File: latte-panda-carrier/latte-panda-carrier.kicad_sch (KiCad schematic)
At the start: 6 parts

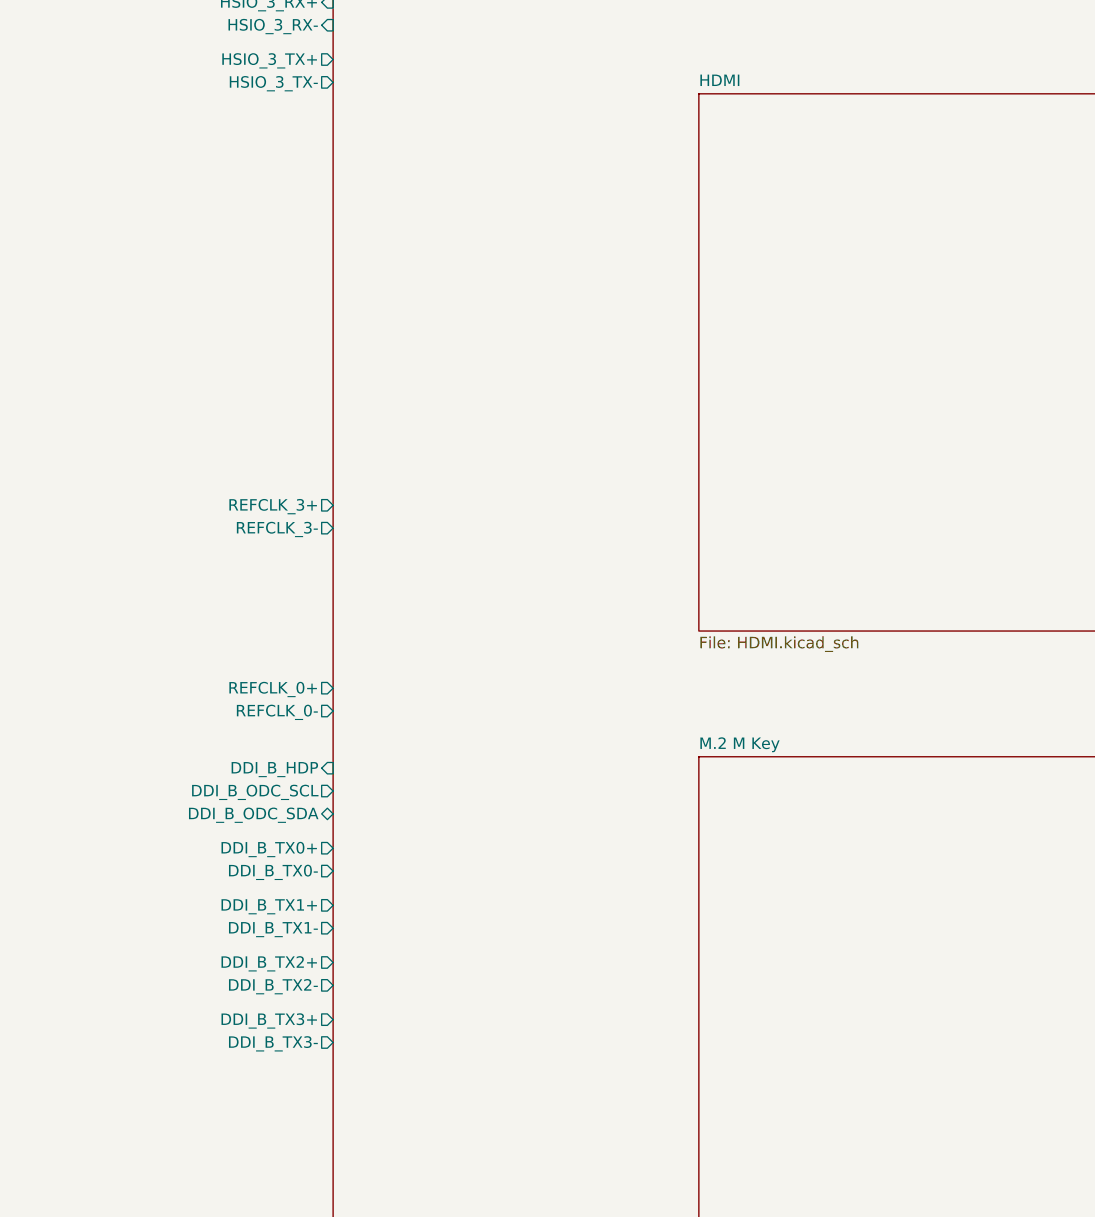
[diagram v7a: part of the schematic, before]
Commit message: 170.2
Add HDMI.
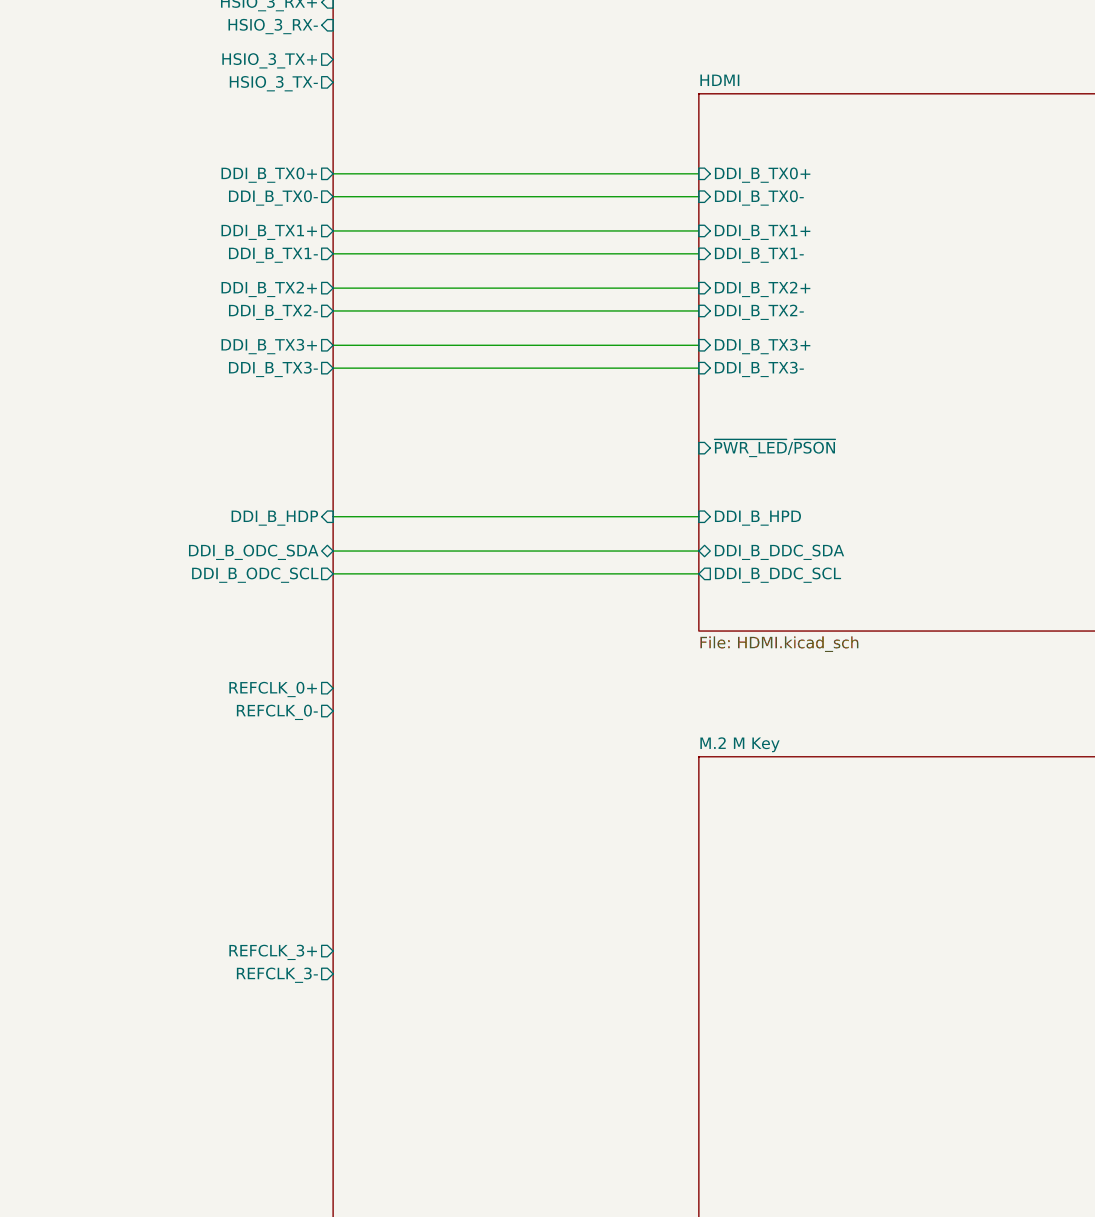
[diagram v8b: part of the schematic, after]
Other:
- sheet HDMI ports: added DDI_B_DDC_SCL, DDI_B_DDC_SDA, DDI_B_HPD, DDI_B_TX0+, DDI_B_TX0-, DDI_B_TX1+, DDI_B_TX1-, DDI_B_TX2+, DDI_B_TX2-, DDI_B_TX3+, DDI_B_TX3-, ~{PWR_LED}/~{PSON}; removed none
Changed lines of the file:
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@@
+	(wire
+		(pts
+			(xy 340.36 283.21) (xy 381 283.21)
+		)
+		(stroke
+			(width 0)
+			(type default)
+		)
+	)
 	(wire
 		(pts
@@
 	(wire
 		(pts
+			(xy 340.36 247.65) (xy 381 247.65)
+		)
+		(stroke
+			(width 0)
+			(type default)
+		)
+	)
+	(wire
+		(pts
 			(xy 340.36 154.94) (xy 381 154.94)
 		)
@@
 	(wire
 		(pts
+			(xy 340.36 243.84) (xy 381 243.84)
+		)
+		(stroke
+			(width 0)
+			(type default)
+		)
+	)
+	(wire
+		(pts
+			(xy 340.36 256.54) (xy 381 256.54)
+		)
+		(stroke
+			(width 0)
+			(type default)
+		)
+	)
+	(wire
+		(pts
 			(xy 184.15 156.21) (xy 217.17 156.21)
 		)
@@
 	(wire
 		(pts
+			(xy 340.36 250.19) (xy 381 250.19)
+		)
+		(stroke
+			(width 0)
+			(type default)
+		)
+	)
+	(wire
+		(pts
 			(xy 184.15 295.91) (xy 217.17 295.91)
 		)
@@
 	(wire
 		(pts
+			(xy 340.36 241.3) (xy 381 241.3)
+		)
+		(stroke
+			(width 0)
+			(type default)
+		)
+	)
+	(wire
+		(pts
 			(xy 184.15 207.01) (xy 217.17 207.01)
 		)
@@
 	(wire
 		(pts
+			(xy 340.36 279.4) (xy 381 279.4)
+		)
+		(stroke
+			(width 0)
+			(type default)
+		)
+	)
+	(wire
+		(pts
 			(xy 340.36 138.43) (xy 381 138.43)
 		)
@@
 	(wire
 		(pts
+			(xy 340.36 260.35) (xy 381 260.35)
+		)
+		(stroke
+			(width 0)
+			(type default)
+		)
+	)
+	(wire
+		(pts
 			(xy 340.36 158.75) (xy 381 158.75)
 		)
@@
 	(wire
 		(pts
+			(xy 340.36 262.89) (xy 381 262.89)
+		)
+		(stroke
+			(width 0)
+			(type default)
+		)
+	)
+	(wire
+		(pts
 			(xy 340.36 91.44) (xy 381 91.44)
 		)
@@
 	(wire
 		(pts
+			(xy 340.36 285.75) (xy 381 285.75)
+		)
+		(stroke
+			(width 0)
+			(type default)
+		)
+	)
+	(wire
+		(pts
 			(xy 184.15 163.83) (xy 217.17 163.83)
+		)
+		(stroke
+			(width 0)
+			(type default)
+		)
+	)
+	(wire
+		(pts
+			(xy 340.36 254) (xy 381 254)
 		)
 		(stroke
@@
 			)
 		)
+		(pin "DDI_B_DDC_SCL" output
+			(at 381 285.75 180)
+			(effects
+				(font
+					(size 1.27 1.27)
+				)
+				(justify left)
+			)
+		)
+		(pin "DDI_B_DDC_SDA" bidirectional
+			(at 381 283.21 180)
+			(effects
+				(font
+					(size 1.27 1.27)
+				)
+				(justify left)
+			)
+		)
+		(pin "DDI_B_HPD" input
+			(at 381 279.4 180)
+			(effects
+				(font
+					(size 1.27 1.27)
+				)
+				(justify left)
+			)
+		)
+		(pin "DDI_B_TX0+" input
+			(at 381 241.3 180)
+			(effects
+				(font
+					(size 1.27 1.27)
+				)
+				(justify left)
+			)
+		)
+		(pin "DDI_B_TX0-" input
+			(at 381 243.84 180)
+			(effects
+				(font
+					(size 1.27 1.27)
+				)
+				(justify left)
+			)
+		)
+		(pin "DDI_B_TX1+" input
+			(at 381 247.65 180)
+			(effects
+				(font
+					(size 1.27 1.27)
+				)
+				(justify left)
+			)
+		)
+		(pin "DDI_B_TX1-" input
+			(at 381 250.19 180)
+			(effects
+				(font
+					(size 1.27 1.27)
+				)
+				(justify left)
+			)
+		)
+		(pin "DDI_B_TX2+" input
+			(at 381 254 180)
+			(effects
+				(font
+					(size 1.27 1.27)
+				)
+				(justify left)
+			)
+		)
+		(pin "DDI_B_TX2-" input
+			(at 381 256.54 180)
+			(effects
+				(font
+					(size 1.27 1.27)
+				)
+				(justify left)
+			)
+		)
+		(pin "DDI_B_TX3+" input
+			(at 381 260.35 180)
+			(effects
+				(font
+					(size 1.27 1.27)
+				)
+				(justify left)
+			)
+		)
+		(pin "DDI_B_TX3-" input
+			(at 381 262.89 180)
+			(effects
+				(font
+					(size 1.27 1.27)
+				)
+				(justify left)
+			)
+		)
+		(pin "~{PWR_LED}{slash}~{PSON}" input
+			(at 381 271.78 180)
+			(effects
+				(font
+					(size 1.27 1.27)
+				)
+				(justify left)
+			)
+		)
 		(instances
 			(project "latte-panda-carrier"
@@
 		)
 		(pin "DDI_B_HDP" input
-			(at 340.36 307.34 0)
+			(at 340.36 279.4 0)
 			(effects
 				(font
@@
 		)
 		(pin "DDI_B_ODC_SCL" output
-			(at 340.36 309.88 0)
+			(at 340.36 285.75 0)
 			(effects
 				(font
@@
 		)
 		(pin "DDI_B_ODC_SDA" bidirectional
-			(at 340.36 312.42 0)
+			(at 340.36 283.21 0)
 			(effects
 				(font
@@
 		)
 		(pin "DDI_B_TX0+" output
-			(at 340.36 316.23 0)
+			(at 340.36 241.3 0)
 			(effects
 				(font
@@
 		)
 		(pin "DDI_B_TX0-" output
-			(at 340.36 318.77 0)
+			(at 340.36 243.84 0)
 			(effects
 				(font
@@
 		)
 		(pin "DDI_B_TX1+" output
-			(at 340.36 322.58 0)
+			(at 340.36 247.65 0)
 			(effects
 				(font
@@
 		)
 		(pin "DDI_B_TX1-" output
-			(at 340.36 325.12 0)
+			(at 340.36 250.19 0)
 			(effects
 				(font
@@
 		)
 		(pin "DDI_B_TX2+" output
-			(at 340.36 328.93 0)
+			(at 340.36 254 0)
 			(effects
 				(font
@@
 		)
 		(pin "DDI_B_TX2-" output
-			(at 340.36 331.47 0)
+			(at 340.36 256.54 0)
 			(effects
 				(font
@@
 		)
 		(pin "DDI_B_TX3+" output
-			(at 340.36 335.28 0)
+			(at 340.36 260.35 0)
 			(effects
 				(font
@@
 		)
 		(pin "DDI_B_TX3-" output
-			(at 340.36 337.82 0)
+			(at 340.36 262.89 0)
 			(effects
 				(font
@@
 		)
 		(pin "REFCLK_3+" output
-			(at 340.36 278.13 0)
+			(at 340.36 327.66 0)
 			(effects
 				(font
@@
 		)
 		(pin "REFCLK_3-" output
-			(at 340.36 280.67 0)
-			(effects
-				(font
+			(at 340.36 330.2 0)
+			(effects
+				(font
